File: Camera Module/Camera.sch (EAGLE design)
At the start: 7 parts, among them U2 RFM69HCW

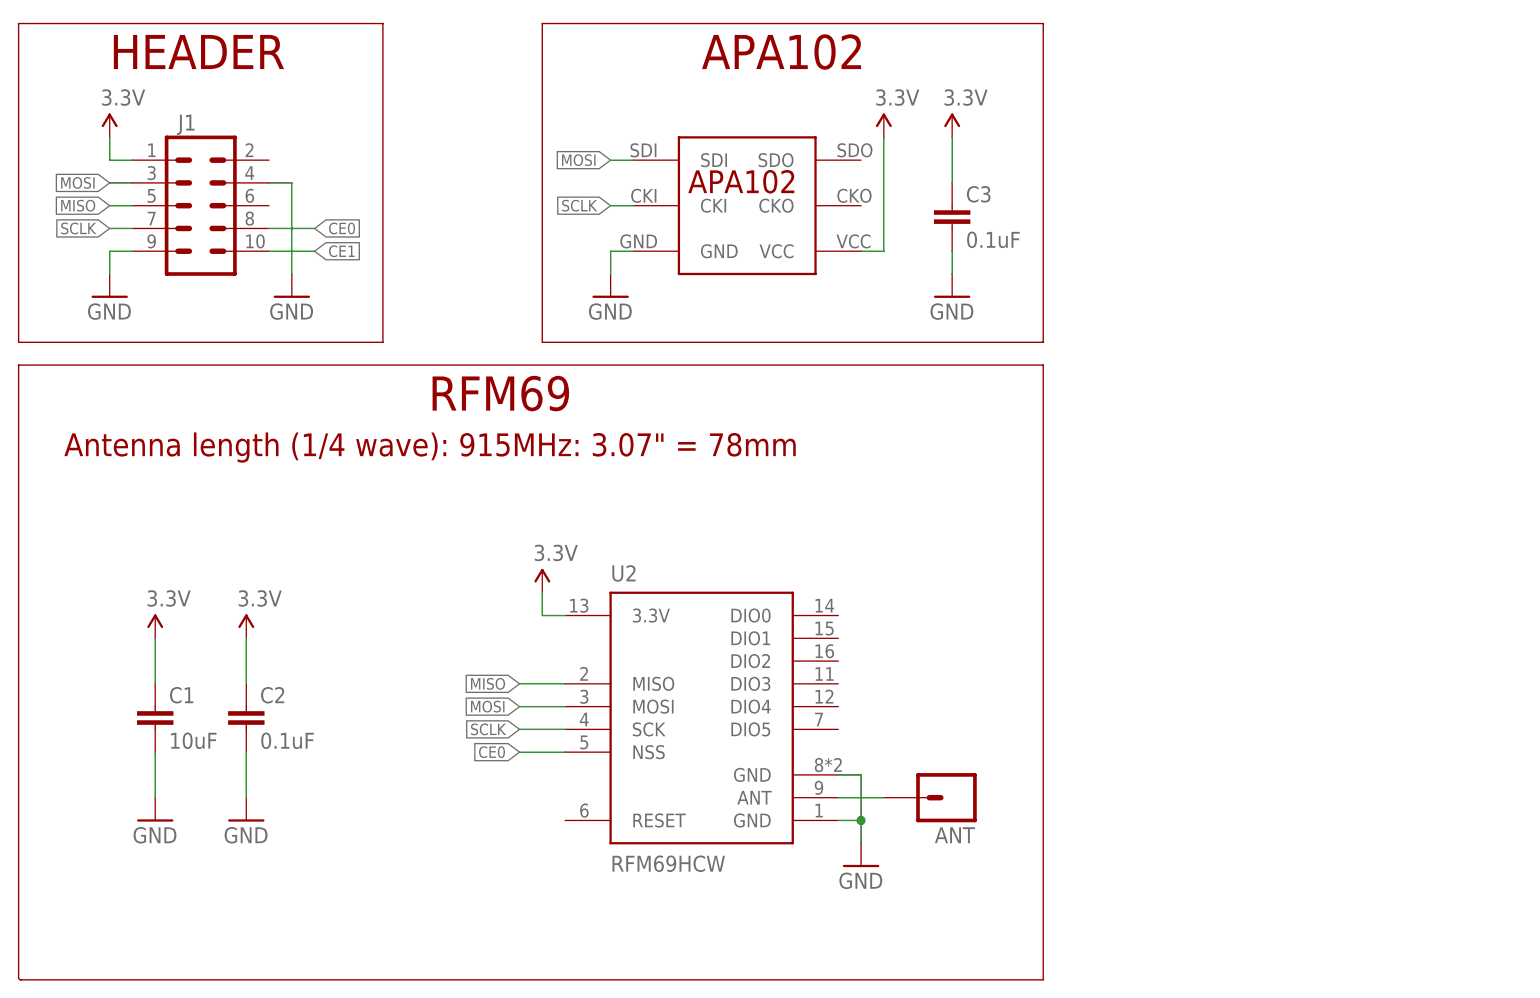
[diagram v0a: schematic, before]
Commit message: Added the interrupt line from the RFM69 into the Camera Module board. It is connected to GPIO_24
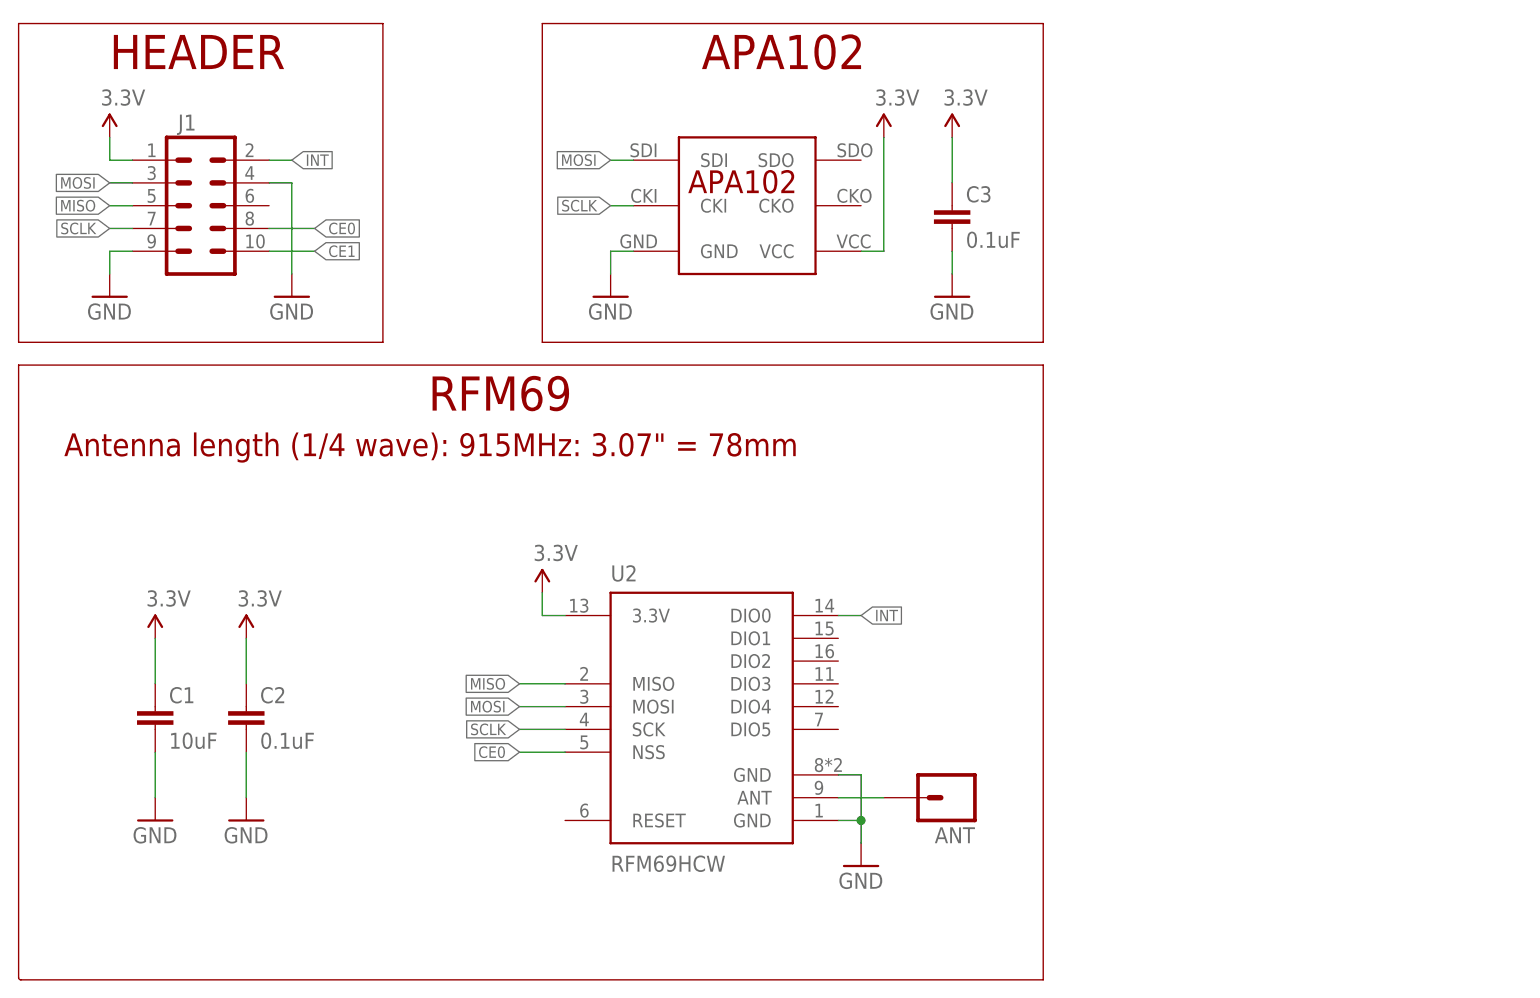
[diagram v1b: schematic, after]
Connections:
- new net INT: J1.2, U2.DIO0
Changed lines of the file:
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@@
+</segment>
+</net>
+<net name="INT" class="0">
+<segment>
+<pinref part="U2" gate="G$1" pin="DIO0"/>
+<wire x1="91.44" y1="40.64" x2="93.98" y2="40.64" width="0.1524" layer="91"/>
+<label x="93.98" y="40.64" size="1.27" layer="95" xref="yes"/>
+</segment>
+<segment>
+<pinref part="J1" gate="G$1" pin="2"/>
+<wire x1="27.94" y1="91.44" x2="30.48" y2="91.44" width="0.1524" layer="91"/>
+<label x="30.48" y="91.44" size="1.27" layer="95" xref="yes"/>
 </segment>
 </net>

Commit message: Update the camera module board to include a chip select line for the APA102 and added to the silk screen
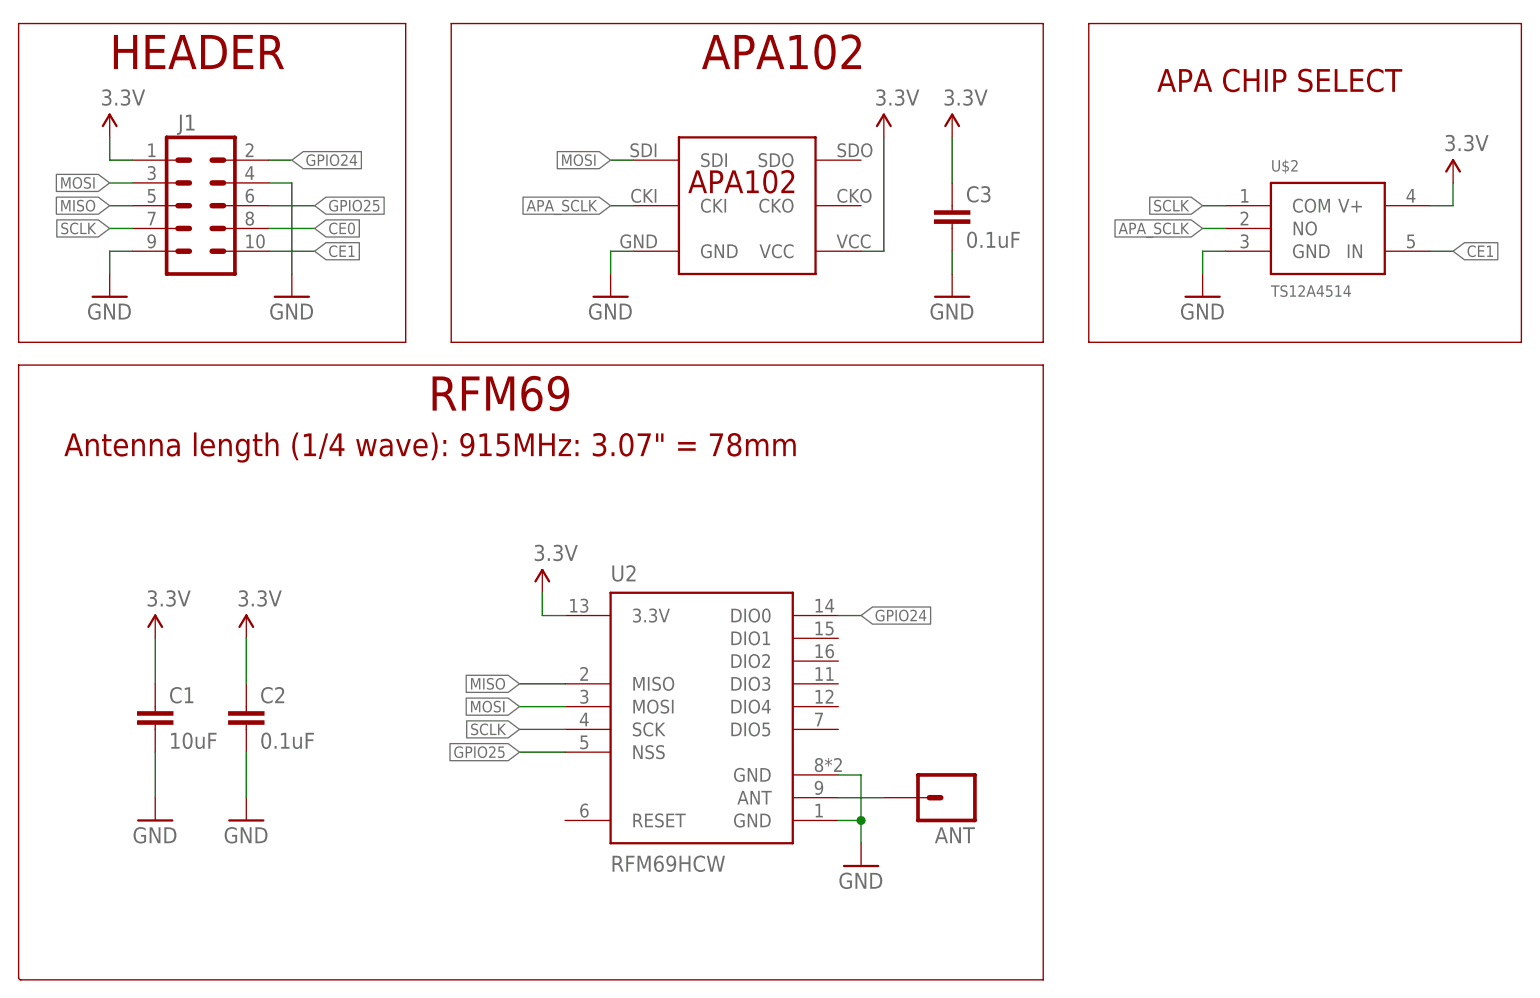
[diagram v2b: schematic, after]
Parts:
- added U$2: TS12A4514, SAUVE:TS12A4514
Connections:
- net INT renamed GPIO24
- new net APA_SCLK: U$1.CKI, U$2.NO
- new net GPIO25: J1.6, U2.NSS
- net 3.3V: now also U$2.V+
- net CE0: no longer U2.NSS
- net CE1: now also U$2.IN
- net GND: now also U$2.GND
- net SCLK: now also U$2.COM; no longer U$1.CKI
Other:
- note added: "APA CHIP SELECT"
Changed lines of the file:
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@@
 <part name="SUPPLY6" library="SparkFun-Aesthetics" deviceset="3.3V" device=""/>
 <part name="GND7" library="SparkFun-Aesthetics" deviceset="GND" device=""/>
+<part name="U$2" library="SAUVE" deviceset="TS12A4514" device=""/>
+<part name="SUPPLY7" library="SparkFun-Aesthetics" deviceset="3.3V" device=""/>
+<part name="GND8" library="SparkFun-Aesthetics" deviceset="GND" device=""/>
 </parts>
 <sheets>
@@
 <text x="45.72" y="63.5" size="3.81" layer="94" ratio="15">RFM69</text>
 <text x="10.16" y="101.6" size="3.81" layer="94">HEADER</text>
-<wire x1="0" y1="106.68" x2="40.64" y2="106.68" width="0.1524" layer="94"/>
-<wire x1="40.64" y1="106.68" x2="40.64" y2="71.12" width="0.1524" layer="94"/>
-<wire x1="40.64" y1="71.12" x2="0" y2="71.12" width="0.1524" layer="94"/>
+<wire x1="0" y1="106.68" x2="43.18" y2="106.68" width="0.1524" layer="94"/>
+<wire x1="43.18" y1="106.68" x2="43.18" y2="71.12" width="0.1524" layer="94"/>
+<wire x1="43.18" y1="71.12" x2="0" y2="71.12" width="0.1524" layer="94"/>
 <wire x1="0" y1="71.12" x2="0" y2="106.68" width="0.1524" layer="94"/>
 <text x="76.2" y="101.6" size="3.81" layer="94">APA102</text>
-<wire x1="58.42" y1="106.68" x2="114.3" y2="106.68" width="0.1524" layer="94"/>
+<wire x1="48.26" y1="106.68" x2="114.3" y2="106.68" width="0.1524" layer="94"/>
 <wire x1="114.3" y1="106.68" x2="114.3" y2="71.12" width="0.1524" layer="94"/>
-<wire x1="114.3" y1="71.12" x2="58.42" y2="71.12" width="0.1524" layer="94"/>
-<wire x1="58.42" y1="71.12" x2="58.42" y2="106.68" width="0.1524" layer="94"/>
+<wire x1="114.3" y1="71.12" x2="48.26" y2="71.12" width="0.1524" layer="94"/>
+<wire x1="48.26" y1="71.12" x2="48.26" y2="106.68" width="0.1524" layer="94"/>
+<wire x1="119.38" y1="106.68" x2="119.38" y2="71.12" width="0.1524" layer="94"/>
+<wire x1="119.38" y1="71.12" x2="167.64" y2="71.12" width="0.1524" layer="94"/>
+<wire x1="167.64" y1="71.12" x2="167.64" y2="106.68" width="0.1524" layer="94"/>
+<wire x1="167.64" y1="106.68" x2="119.38" y2="106.68" width="0.1524" layer="94"/>
+<text x="127" y="99.06" size="2.54" layer="94">APA CHIP SELECT</text>
 </plain>
 <instances>
@@
 <instance part="SUPPLY6" gate="G$1" x="104.14" y="93.98"/>
 <instance part="GND7" gate="1" x="104.14" y="76.2"/>
+<instance part="U$2" gate="G$1" x="144.78" y="83.82"/>
+<instance part="SUPPLY7" gate="G$1" x="160.02" y="88.9"/>
+<instance part="GND8" gate="1" x="132.08" y="76.2"/>
 </instances>
 <busses>
@@
 <wire x1="104.14" y1="78.74" x2="104.14" y2="81.28" width="0.1524" layer="91"/>
 </segment>
+<segment>
+<pinref part="U$2" gate="G$1" pin="GND"/>
+<pinref part="GND8" gate="1" pin="GND"/>
+<wire x1="134.62" y1="81.28" x2="132.08" y2="81.28" width="0.1524" layer="91"/>
+<wire x1="132.08" y1="81.28" x2="132.08" y2="78.74" width="0.1524" layer="91"/>
+</segment>
 </net>
 <net name="3.3V" class="0">
@@
 <wire x1="104.14" y1="93.98" x2="104.14" y2="88.9" width="0.1524" layer="91"/>
 </segment>
+<segment>
+<pinref part="U$2" gate="G$1" pin="V+"/>
+<pinref part="SUPPLY7" gate="G$1" pin="3.3V"/>
+<wire x1="157.48" y1="86.36" x2="160.02" y2="86.36" width="0.1524" layer="91"/>
+<wire x1="160.02" y1="86.36" x2="160.02" y2="88.9" width="0.1524" layer="91"/>
+</segment>
 </net>
 <net name="ANT" class="0">
@@
 </segment>
 <segment>
+<pinref part="U2" gate="G$1" pin="SCK"/>
+<wire x1="55.88" y1="27.94" x2="60.96" y2="27.94" width="0.1524" layer="91"/>
+<label x="55.88" y="27.94" size="1.27" layer="95" rot="R180" xref="yes"/>
+</segment>
+<segment>
+<pinref part="U$2" gate="G$1" pin="COM"/>
+<wire x1="134.62" y1="86.36" x2="132.08" y2="86.36" width="0.1524" layer="91"/>
+<label x="132.08" y="86.36" size="1.27" layer="95" rot="R180" xref="yes"/>
+</segment>
+</net>
+<net name="CE0" class="0">
+<segment>
+<pinref part="J1" gate="G$1" pin="8"/>
+<wire x1="27.94" y1="83.82" x2="33.02" y2="83.82" width="0.1524" layer="91"/>
+<label x="33.02" y="83.82" size="1.27" layer="95" xref="yes"/>
+</segment>
+</net>
+<net name="CE1" class="0">
+<segment>
+<pinref part="J1" gate="G$1" pin="10"/>
+<wire x1="27.94" y1="81.28" x2="33.02" y2="81.28" width="0.1524" layer="91"/>
+<label x="33.02" y="81.28" size="1.27" layer="95" xref="yes"/>
+</segment>
+<segment>
+<pinref part="U$2" gate="G$1" pin="IN"/>
+<wire x1="157.48" y1="81.28" x2="160.02" y2="81.28" width="0.1524" layer="91"/>
+<label x="160.02" y="81.28" size="1.27" layer="95" xref="yes"/>
+</segment>
+</net>
+<net name="GPIO25" class="0">
+<segment>
+<pinref part="J1" gate="G$1" pin="6"/>
+<wire x1="27.94" y1="86.36" x2="33.02" y2="86.36" width="0.1524" layer="91"/>
+<label x="33.02" y="86.36" size="1.27" layer="95" xref="yes"/>
+</segment>
+<segment>
+<pinref part="U2" gate="G$1" pin="NSS"/>
+<wire x1="55.88" y1="25.4" x2="60.96" y2="25.4" width="0.1524" layer="91"/>
+<label x="55.88" y="25.4" size="1.27" layer="95" rot="R180" xref="yes"/>
+</segment>
+</net>
+<net name="GPIO24" class="0">
+<segment>
+<pinref part="J1" gate="G$1" pin="2"/>
+<wire x1="27.94" y1="91.44" x2="30.48" y2="91.44" width="0.1524" layer="91"/>
+<label x="30.48" y="91.44" size="1.27" layer="95" xref="yes"/>
+</segment>
+<segment>
+<pinref part="U2" gate="G$1" pin="DIO0"/>
+<wire x1="91.44" y1="40.64" x2="93.98" y2="40.64" width="0.1524" layer="91"/>
+<label x="93.98" y="40.64" size="1.27" layer="95" xref="yes"/>
+</segment>
+</net>
+<net name="APA_SCLK" class="0">
+<segment>
 <pinref part="U$1" gate="G$1" pin="CKI"/>
 <wire x1="68.58" y1="86.36" x2="66.04" y2="86.36" width="0.1524" layer="91"/>
@@
 </segment>
 <segment>
-<pinref part="U2" gate="G$1" pin="SCK"/>
-<wire x1="55.88" y1="27.94" x2="60.96" y2="27.94" width="0.1524" layer="91"/>
-<label x="55.88" y="27.94" size="1.27" layer="95" rot="R180" xref="yes"/>
-</segment>
-</net>
-<net name="CE0" class="0">
-<segment>
-<pinref part="J1" gate="G$1" pin="8"/>
-<wire x1="27.94" y1="83.82" x2="33.02" y2="83.82" width="0.1524" layer="91"/>
-<label x="33.02" y="83.82" size="1.27" layer="95" xref="yes"/>
-</segment>
-<segment>
-<pinref part="U2" gate="G$1" pin="NSS"/>
-<wire x1="55.88" y1="25.4" x2="60.96" y2="25.4" width="0.1524" layer="91"/>
-<label x="55.88" y="25.4" size="1.27" layer="95" rot="R180" xref="yes"/>
-</segment>
-</net>
-<net name="CE1" class="0">
-<segment>
-<pinref part="J1" gate="G$1" pin="10"/>
-<wire x1="27.94" y1="81.28" x2="33.02" y2="81.28" width="0.1524" layer="91"/>
-<label x="33.02" y="81.28" size="1.27" layer="95" xref="yes"/>
-</segment>
-</net>
-<net name="INT" class="0">
-<segment>
-<pinref part="U2" gate="G$1" pin="DIO0"/>
-<wire x1="91.44" y1="40.64" x2="93.98" y2="40.64" width="0.1524" layer="91"/>
-<label x="93.98" y="40.64" size="1.27" layer="95" xref="yes"/>
-</segment>
-<segment>
-<pinref part="J1" gate="G$1" pin="2"/>
-<wire x1="27.94" y1="91.44" x2="30.48" y2="91.44" width="0.1524" layer="91"/>
-<label x="30.48" y="91.44" size="1.27" layer="95" xref="yes"/>
-</segment>
-</net>
+<pinref part="U$2" gate="G$1" pin="NO"/>
+<wire x1="134.62" y1="83.82" x2="132.08" y2="83.82" width="0.1524" layer="91"/>
+<label x="132.08" y="83.82" size="1.27" layer="95" rot="R180" xref="yes"/>
+</segment>
+</net>

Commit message: Finalized all PCBs
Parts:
- added JP1: JUMPER-PAD-2-NC_BY_TRACE, SparkFun-Passives:JUMPER-PAD-2-NC_BY_TRACE
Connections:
- net APA_SCLK: now also JP1.2
- net SCLK: now also JP1.1
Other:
- moved on the sheet: C3
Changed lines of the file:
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@@
 <part name="SUPPLY7" library="SparkFun-Aesthetics" deviceset="3.3V" device=""/>
 <part name="GND8" library="SparkFun-Aesthetics" deviceset="GND" device=""/>
+<part name="JP1" library="SparkFun-Passives" deviceset="JUMPER-PAD-2-NC_BY_TRACE" device=""/>
 </parts>
 <sheets>
@@
 <wire x1="43.18" y1="71.12" x2="0" y2="71.12" width="0.1524" layer="94"/>
 <wire x1="0" y1="71.12" x2="0" y2="106.68" width="0.1524" layer="94"/>
-<text x="76.2" y="101.6" size="3.81" layer="94">APA102</text>
-<wire x1="48.26" y1="106.68" x2="114.3" y2="106.68" width="0.1524" layer="94"/>
-<wire x1="114.3" y1="106.68" x2="114.3" y2="71.12" width="0.1524" layer="94"/>
-<wire x1="114.3" y1="71.12" x2="48.26" y2="71.12" width="0.1524" layer="94"/>
-<wire x1="48.26" y1="71.12" x2="48.26" y2="106.68" width="0.1524" layer="94"/>
+<text x="78.74" y="101.6" size="3.81" layer="94">APA102</text>
+<wire x1="45.72" y1="106.68" x2="116.84" y2="106.68" width="0.1524" layer="94"/>
+<wire x1="116.84" y1="106.68" x2="116.84" y2="71.12" width="0.1524" layer="94"/>
+<wire x1="116.84" y1="71.12" x2="45.72" y2="71.12" width="0.1524" layer="94"/>
+<wire x1="45.72" y1="71.12" x2="45.72" y2="106.68" width="0.1524" layer="94"/>
 <wire x1="119.38" y1="106.68" x2="119.38" y2="71.12" width="0.1524" layer="94"/>
 <wire x1="119.38" y1="71.12" x2="167.64" y2="71.12" width="0.1524" layer="94"/>
@@
 <instance part="GND4" gate="1" x="10.16" y="76.2"/>
 <instance part="GND5" gate="1" x="30.48" y="76.2"/>
-<instance part="U$1" gate="G$1" x="81.28" y="86.36"/>
-<instance part="GND6" gate="1" x="66.04" y="76.2"/>
-<instance part="SUPPLY5" gate="G$1" x="96.52" y="93.98"/>
-<instance part="C3" gate="G$1" x="104.14" y="83.82"/>
-<instance part="SUPPLY6" gate="G$1" x="104.14" y="93.98"/>
-<instance part="GND7" gate="1" x="104.14" y="76.2"/>
+<instance part="U$1" gate="G$1" x="83.82" y="86.36"/>
+<instance part="GND6" gate="1" x="68.58" y="76.2"/>
+<instance part="SUPPLY5" gate="G$1" x="99.06" y="93.98"/>
+<instance part="C3" gate="G$1" x="106.68" y="83.82"/>
+<instance part="SUPPLY6" gate="G$1" x="106.68" y="93.98"/>
+<instance part="GND7" gate="1" x="106.68" y="76.2"/>
 <instance part="U$2" gate="G$1" x="144.78" y="83.82"/>
 <instance part="SUPPLY7" gate="G$1" x="160.02" y="88.9"/>
 <instance part="GND8" gate="1" x="132.08" y="76.2"/>
+<instance part="JP1" gate="G$1" x="60.96" y="81.28" smashed="yes"/>
 </instances>
 <busses>
@@
 <segment>
 <pinref part="U$1" gate="G$1" pin="GND"/>
-<wire x1="68.58" y1="81.28" x2="66.04" y2="81.28" width="0.1524" layer="91"/>
+<wire x1="71.12" y1="81.28" x2="68.58" y2="81.28" width="0.1524" layer="91"/>
 <pinref part="GND6" gate="1" pin="GND"/>
-<wire x1="66.04" y1="81.28" x2="66.04" y2="78.74" width="0.1524" layer="91"/>
+<wire x1="68.58" y1="81.28" x2="68.58" y2="78.74" width="0.1524" layer="91"/>
 </segment>
 <segment>
 <pinref part="C3" gate="G$1" pin="2"/>
 <pinref part="GND7" gate="1" pin="GND"/>
-<wire x1="104.14" y1="78.74" x2="104.14" y2="81.28" width="0.1524" layer="91"/>
+<wire x1="106.68" y1="78.74" x2="106.68" y2="81.28" width="0.1524" layer="91"/>
 </segment>
 <segment>
@@
 <pinref part="U$1" gate="G$1" pin="VCC"/>
 <pinref part="SUPPLY5" gate="G$1" pin="3.3V"/>
-<wire x1="93.98" y1="81.28" x2="96.52" y2="81.28" width="0.1524" layer="91"/>
-<wire x1="96.52" y1="81.28" x2="96.52" y2="93.98" width="0.1524" layer="91"/>
+<wire x1="96.52" y1="81.28" x2="99.06" y2="81.28" width="0.1524" layer="91"/>
+<wire x1="99.06" y1="81.28" x2="99.06" y2="93.98" width="0.1524" layer="91"/>
 </segment>
 <segment>
 <pinref part="C3" gate="G$1" pin="1"/>
 <pinref part="SUPPLY6" gate="G$1" pin="3.3V"/>
-<wire x1="104.14" y1="93.98" x2="104.14" y2="88.9" width="0.1524" layer="91"/>
+<wire x1="106.68" y1="93.98" x2="106.68" y2="88.9" width="0.1524" layer="91"/>
 </segment>
 <segment>
@@
 <segment>
 <pinref part="U$1" gate="G$1" pin="SDI"/>
-<wire x1="68.58" y1="91.44" x2="66.04" y2="91.44" width="0.1524" layer="91"/>
-<label x="66.04" y="91.44" size="1.27" layer="95" rot="R180" xref="yes"/>
+<wire x1="71.12" y1="91.44" x2="68.58" y2="91.44" width="0.1524" layer="91"/>
+<label x="68.58" y="91.44" size="1.27" layer="95" rot="R180" xref="yes"/>
 </segment>
 <segment>
@@
 <label x="132.08" y="86.36" size="1.27" layer="95" rot="R180" xref="yes"/>
 </segment>
+<segment>
+<pinref part="JP1" gate="G$1" pin="1"/>
+<wire x1="55.88" y1="81.28" x2="53.34" y2="81.28" width="0.1524" layer="91"/>
+<label x="53.34" y="81.28" size="1.27" layer="95" rot="R180" xref="yes"/>
+</segment>
 </net>
 <net name="CE0" class="0">
@@
 <segment>
 <pinref part="U$1" gate="G$1" pin="CKI"/>
-<wire x1="68.58" y1="86.36" x2="66.04" y2="86.36" width="0.1524" layer="91"/>
-<label x="66.04" y="86.36" size="1.27" layer="95" rot="R180" xref="yes"/>
-</segment>
-<segment>
+<wire x1="71.12" y1="86.36" x2="66.04" y2="86.36" width="0.1524" layer="91"/>
+<label x="58.42" y="86.36" size="1.27" layer="95" rot="R180" xref="yes"/>
+<pinref part="JP1" gate="G$1" pin="2"/>
+<wire x1="66.04" y1="86.36" x2="58.42" y2="86.36" width="0.1524" layer="91"/>
+<wire x1="66.04" y1="86.36" x2="66.04" y2="81.28" width="0.1524" layer="91"/>
+<junction x="66.04" y="86.36"/>
+</segment>
+<segment>
